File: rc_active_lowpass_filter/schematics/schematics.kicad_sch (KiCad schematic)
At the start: 14 parts, among them U1 LM741, U2 LM741

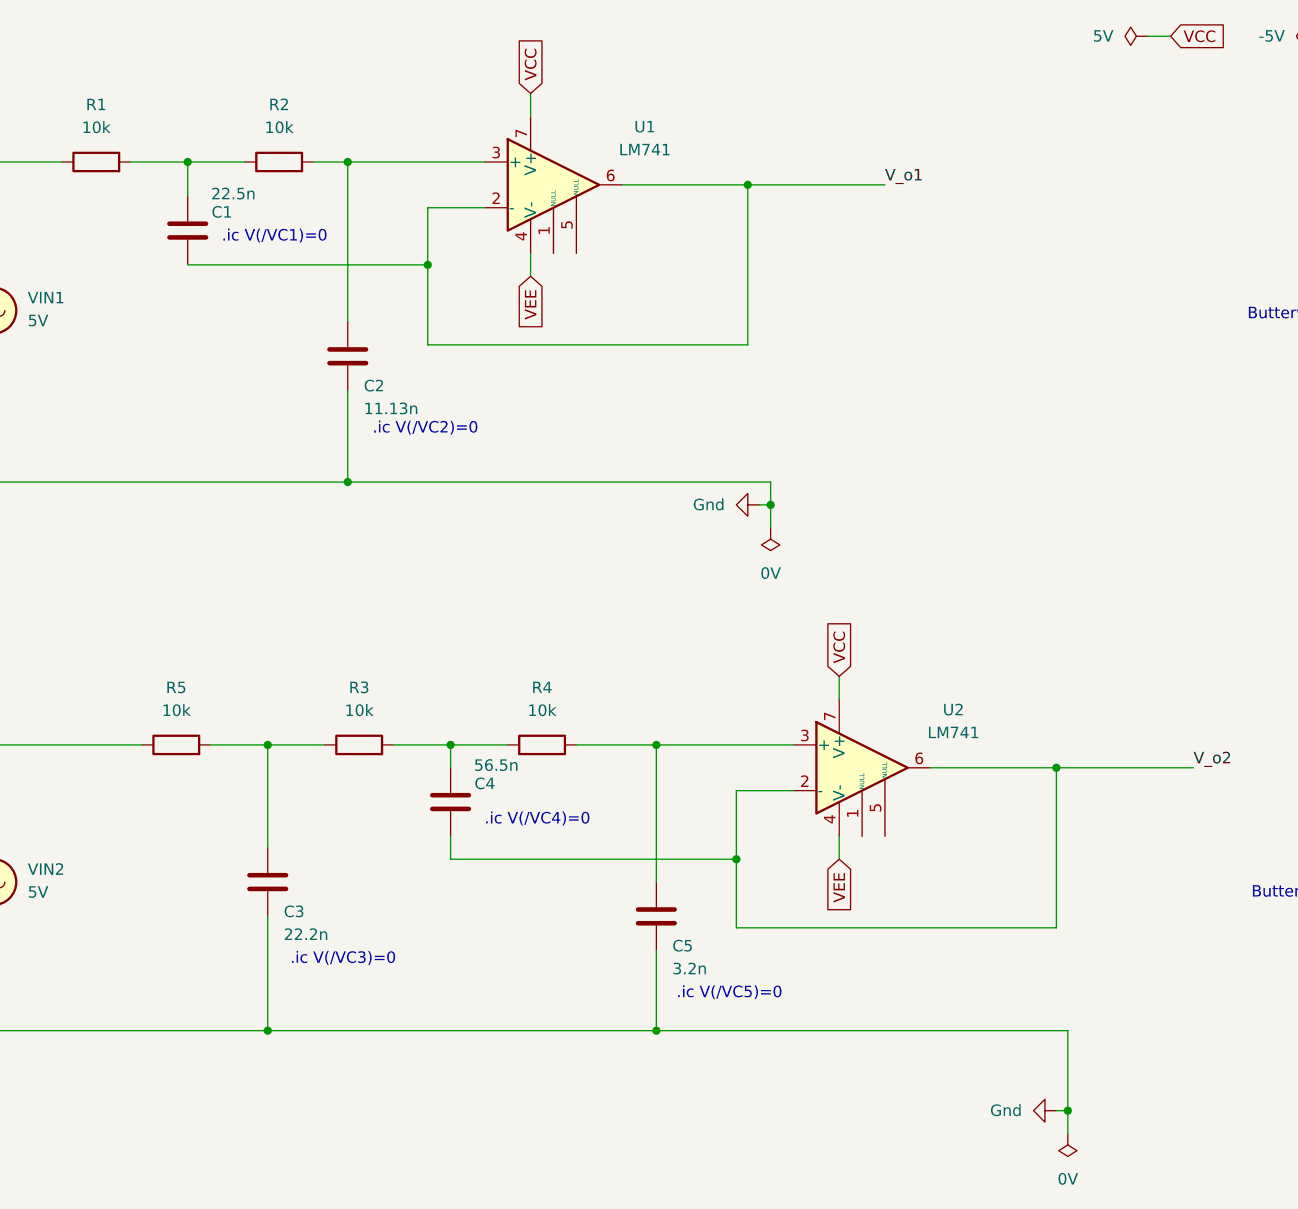
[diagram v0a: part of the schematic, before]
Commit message: feat: Add RC active lowpass filter documentation and schematics
Adds simulation and updated values for schematics based on calculations
for 2-pole and 3-pole RC filters.

Issue found simulating 2-pole filter. The output does not match expected
values. Further investigation needed.

Breaking changes: None

Resolves: None
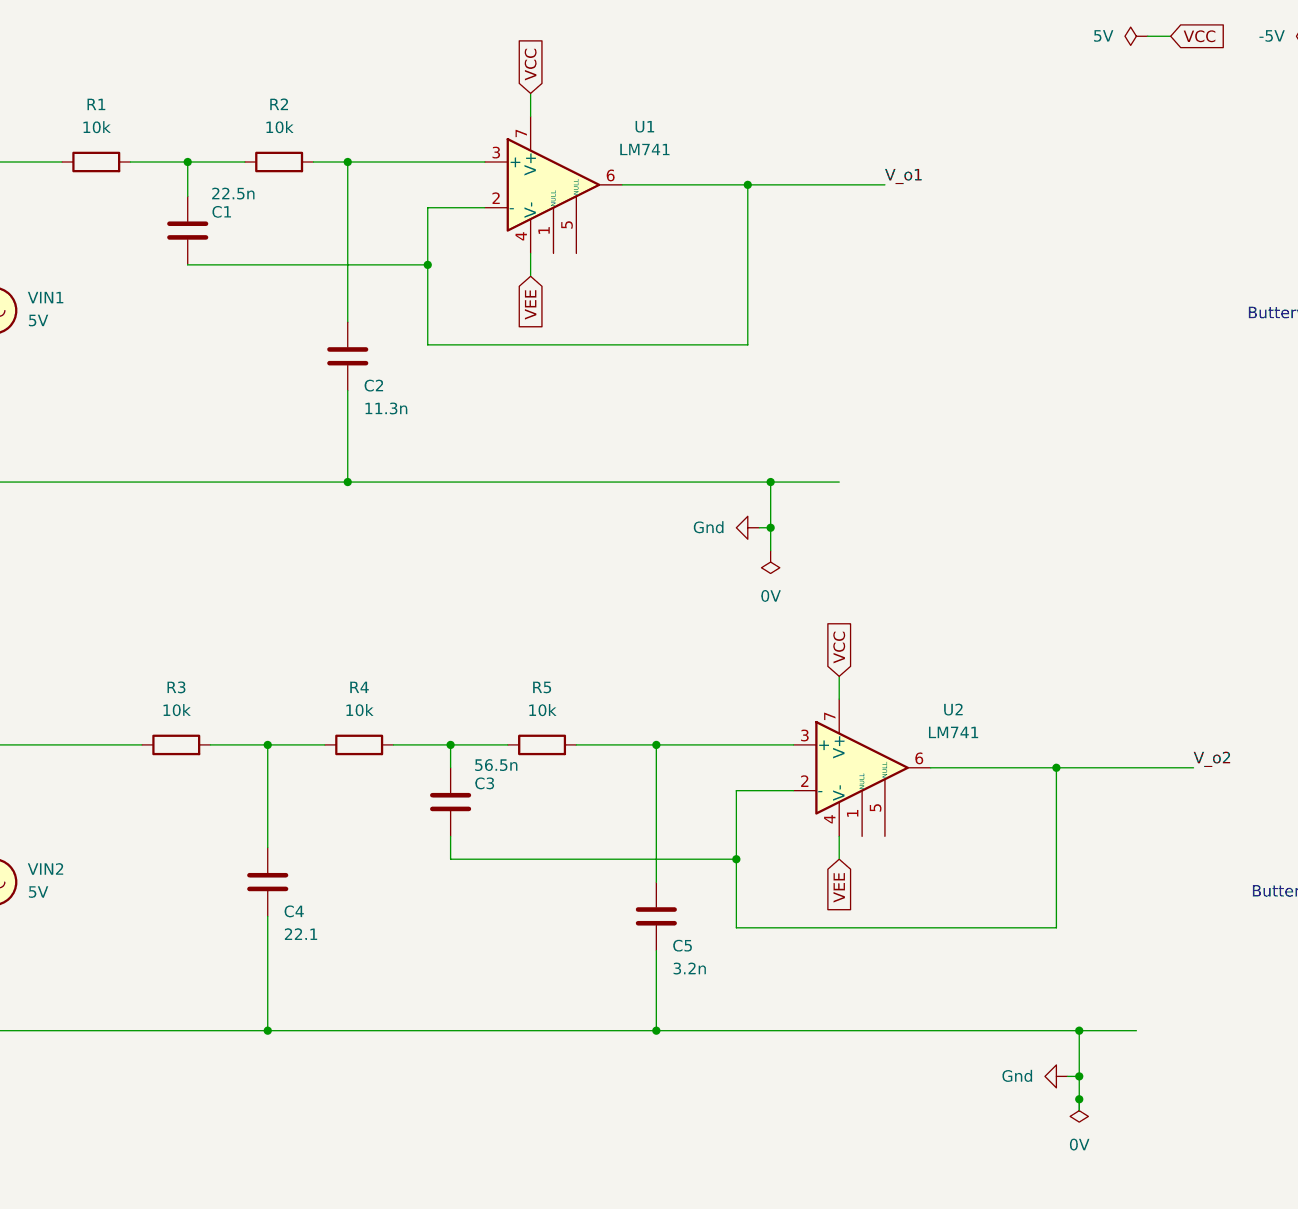
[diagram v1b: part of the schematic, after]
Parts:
- C2: value 11.13n -> 11.3n
- C4: renamed from C3; value 22.2n -> 22.1
- renumbered C4 to C3, R5 to R3, R3 to R4, R4 to R5
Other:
- note removed: ".ic V(/VC1)=0"
- note removed: ".ic V(/VC2)=0"
- note removed: ".ic V(/VC3)=0"
- note removed: ".ic V(/VC4)=0"
- note removed: ".ic V(/VC5)=0"

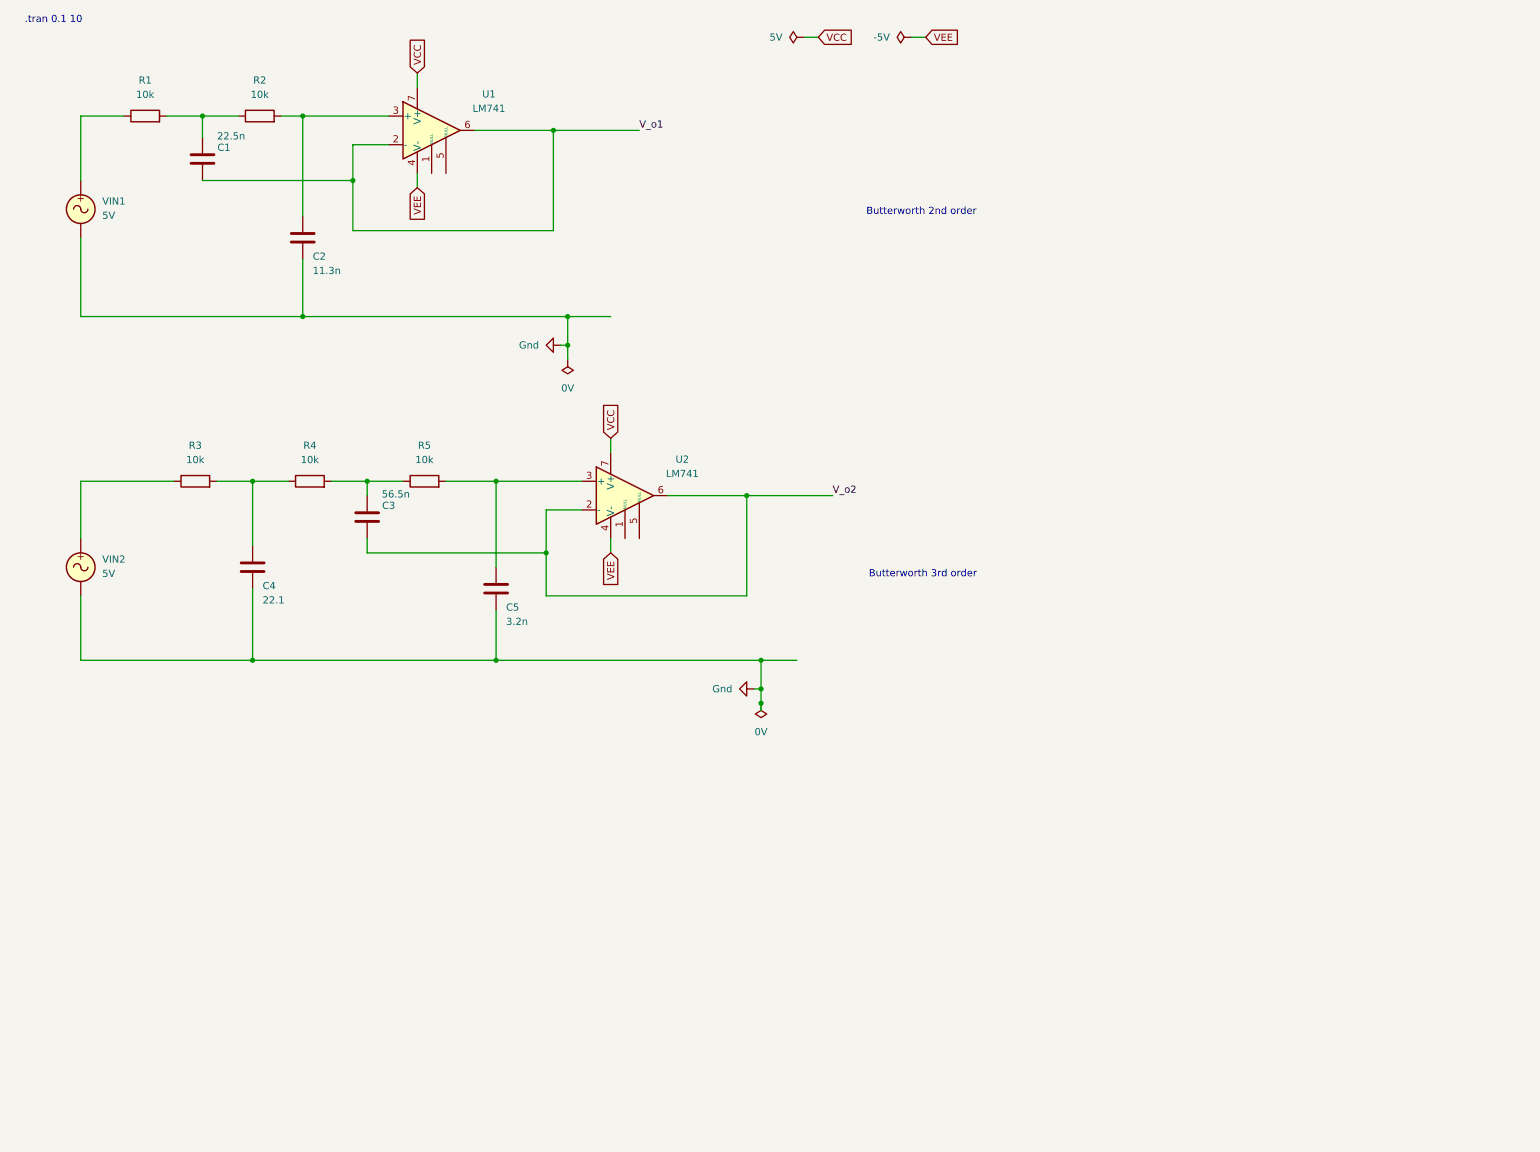
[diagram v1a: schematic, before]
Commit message: feat: Add 5th order RC active low-pass filter design
Adds a 5th order RC active low-pass filter design to the repository.
Includes schematics, simulation results, and a adds description of the
design in the readme.

Minor changes to the readme formatting for better clarity.

Breaking changes: None

Resolves: None
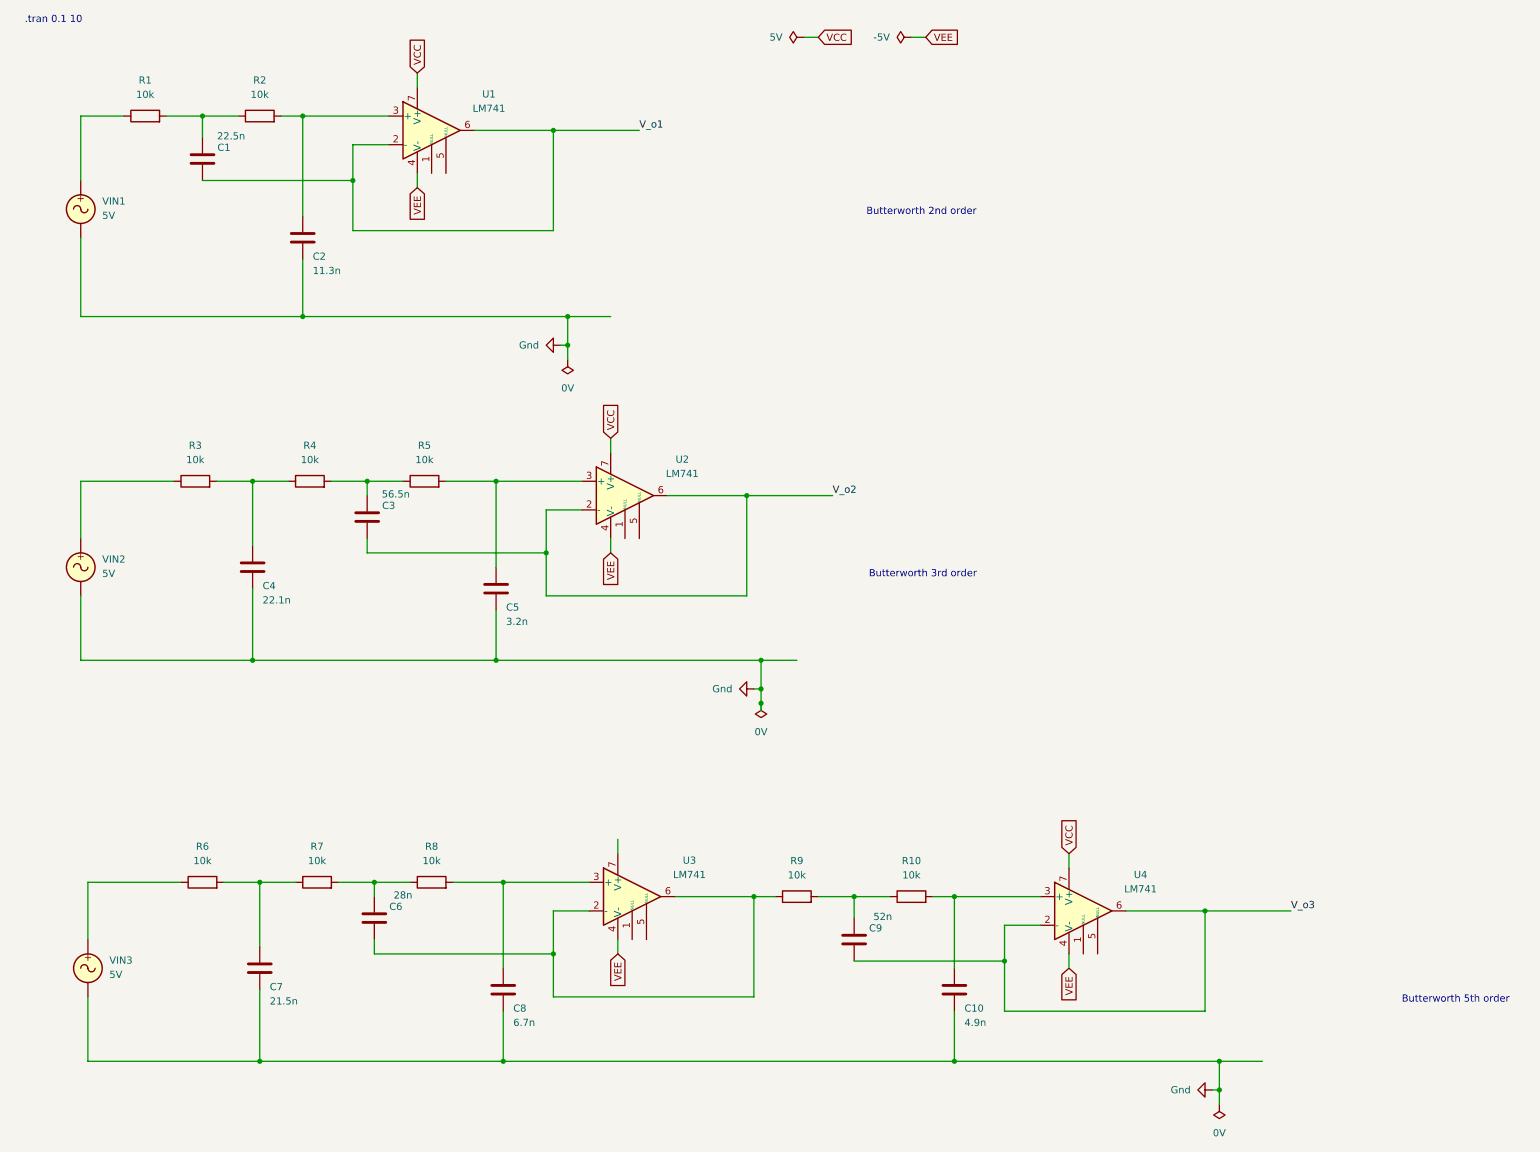
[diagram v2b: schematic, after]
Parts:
- added C10: 4.9n, symbol Device:C
- added C6: 28n, symbol Device:C
- added C7: 21.5n, symbol Device:C
- added C8: 6.7n, symbol Device:C
- added C9: 52n, symbol Device:C
- added R10, R6, R7, R8, R9: 10k, symbol Device:R
- added U3, U4: LM741, symbol Amplifier_Operational:LM741
- added VIN3: 5V, symbol Simulation_SPICE:VSIN
- C4: value 22.1 -> 22.1n
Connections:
- net Gnd: now also C10.2, C7.2, C8.2, VIN3.2
- net VCC: now also U4.7 (V+)
- net VEE: now also U3.4 (V-), U4.4 (V-)
- new net: C9.2, R10.1, R9.2
- new net: C10.1, R10.2, U4.3 (+)
- new net: C7.1, R6.2, R7.1
- new net: C6.2, R7.2, R8.1
- new net: R6.1, VIN3.1
- new net: C6.1, R9.1, U3.2 (-), U3.6
- new net: C8.1, R8.2, U3.3 (+)
- new net V_o3: C9.1, U4.2 (-), U4.6
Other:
- note added: "Butterworth 5th order"
